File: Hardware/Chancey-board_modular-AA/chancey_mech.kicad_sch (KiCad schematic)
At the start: 81 parts

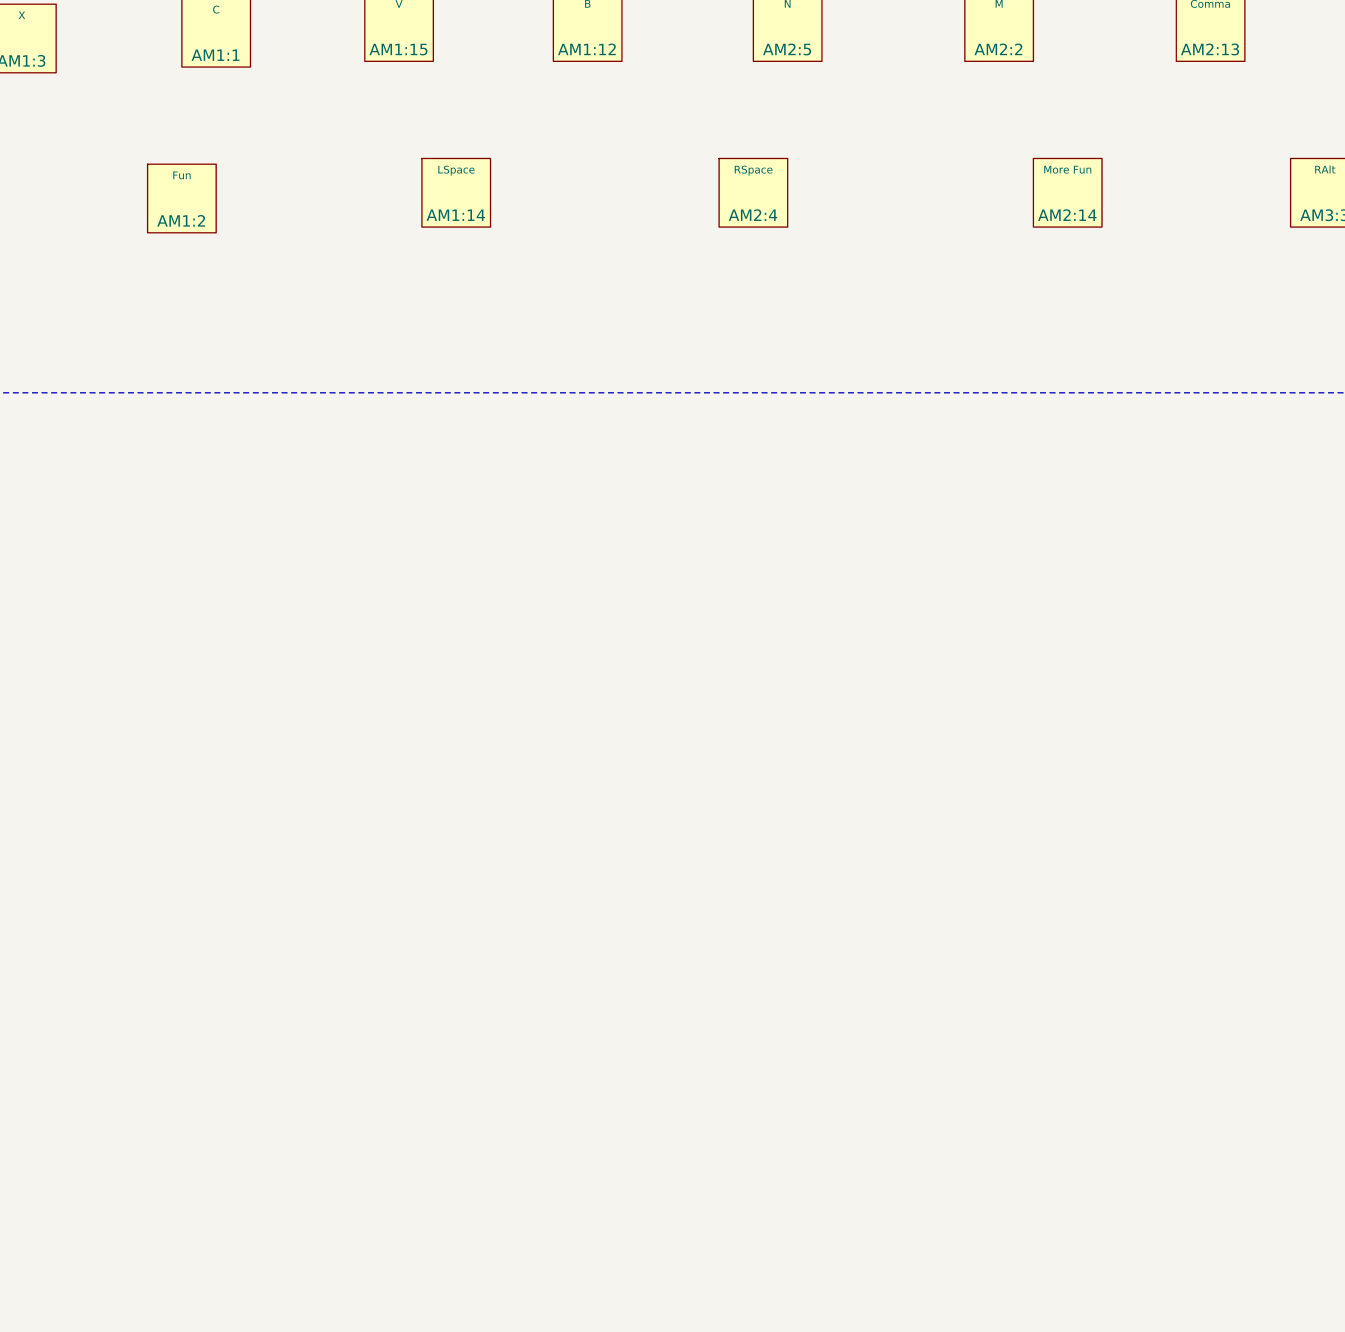
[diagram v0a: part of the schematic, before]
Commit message: Changed many global labels to hierarchical and local labels.
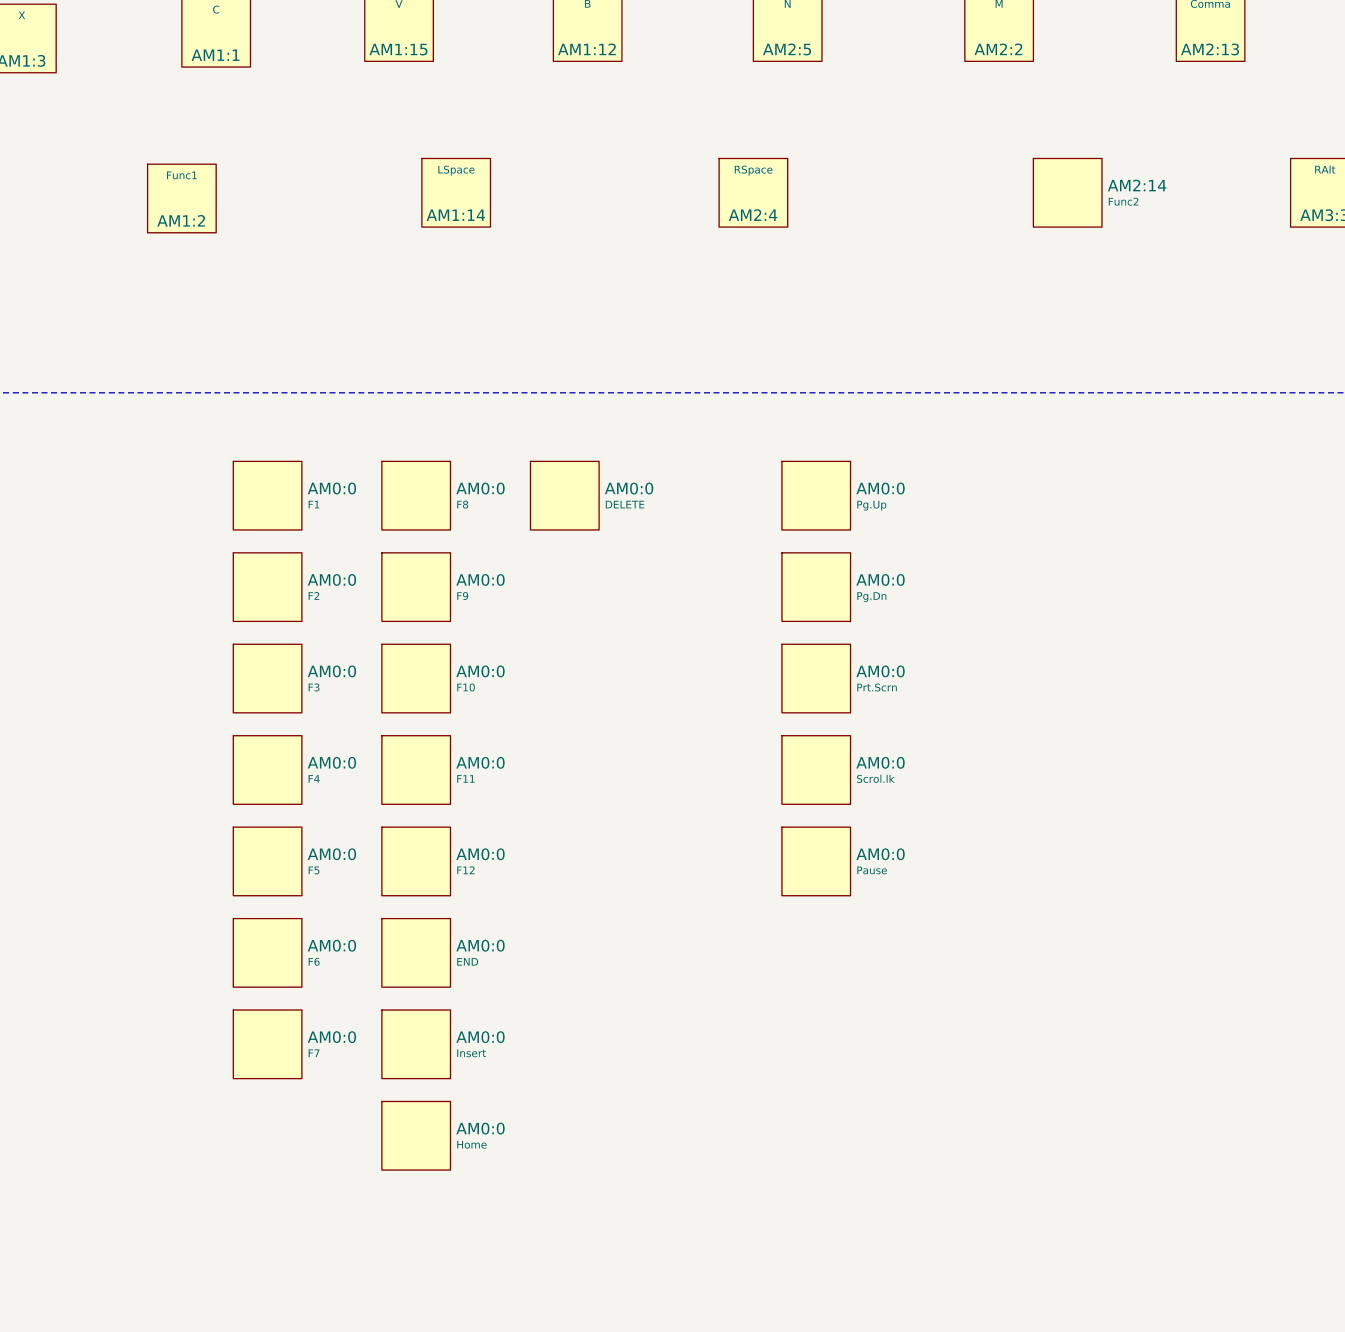
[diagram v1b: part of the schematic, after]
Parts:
- added AM0:0: F3, Chancey_modular:VoidSwitch_1u_SMD, symbol voidswitch:VoidSwitch
- added AM0:0: DELETE, Chancey_modular:VoidSwitch_1u_SMD, symbol voidswitch:VoidSwitch
- added AM0:0: F4, Chancey_modular:VoidSwitch_1u_SMD, symbol voidswitch:VoidSwitch
- added AM0:0: Home, Chancey_modular:VoidSwitch_1u_SMD, symbol voidswitch:VoidSwitch
- added AM0:0: F6, Chancey_modular:VoidSwitch_1u_SMD, symbol voidswitch:VoidSwitch
- added AM0:0: F5, Chancey_modular:VoidSwitch_1u_SMD, symbol voidswitch:VoidSwitch
- added AM0:0: Prt.Scrn, Chancey_modular:VoidSwitch_1u_SMD, symbol voidswitch:VoidSwitch
- added AM0:0: F2, Chancey_modular:VoidSwitch_1u_SMD, symbol voidswitch:VoidSwitch
- added AM0:0: Scrol.lk, Chancey_modular:VoidSwitch_1u_SMD, symbol voidswitch:VoidSwitch
- added AM0:0: Pause, Chancey_modular:VoidSwitch_1u_SMD, symbol voidswitch:VoidSwitch
- added AM0:0: Pg.Dn, Chancey_modular:VoidSwitch_1u_SMD, symbol voidswitch:VoidSwitch
- added AM0:0: F11, Chancey_modular:VoidSwitch_1u_SMD, symbol voidswitch:VoidSwitch
- added AM0:0: F10, Chancey_modular:VoidSwitch_1u_SMD, symbol voidswitch:VoidSwitch
- added AM0:0: END, Chancey_modular:VoidSwitch_1u_SMD, symbol voidswitch:VoidSwitch
- added AM0:0: F9, Chancey_modular:VoidSwitch_1u_SMD, symbol voidswitch:VoidSwitch
- added AM0:0: F8, Chancey_modular:VoidSwitch_1u_SMD, symbol voidswitch:VoidSwitch
- added AM0:0: F7, Chancey_modular:VoidSwitch_1u_SMD, symbol voidswitch:VoidSwitch
- added AM0:0: F12, Chancey_modular:VoidSwitch_1u_SMD, symbol voidswitch:VoidSwitch
- added AM0:0: Pg.Up, Chancey_modular:VoidSwitch_1u_SMD, symbol voidswitch:VoidSwitch
- added AM0:0: F1, Chancey_modular:VoidSwitch_1u_SMD, symbol voidswitch:VoidSwitch
- added AM0:0: Insert, Chancey_modular:VoidSwitch_1u_SMD, symbol voidswitch:VoidSwitch
- AM0:0, AM0:1, AM0:15, AM3:3: footprint void_switch:VoidSwitch_1.25u_SMD -> Chancey_modular:VoidSwitch_1u_SMD
- AM0:10, AM0:11, AM0:12, AM0:13, AM0:14, AM0:2, AM0:3, AM0:4, AM0:5, AM0:6, AM0:7, AM0:8, AM0:9, AM1:0, AM1:1, AM1:10, AM1:11, AM1:12, AM1:13, AM1:14, AM1:15, AM1:3, AM1:4, AM1:5, AM1:6, AM1:7, AM1:8, AM1:9, AM2:10, AM2:11, AM2:12, AM2:13, AM2:2, AM2:3, AM2:4, AM2:5, AM2:6, AM2:7, AM2:8, AM2:9, AM3:1, AM3:10, AM3:11, AM3:12, AM3:13, AM3:14, AM3:2, AM3:4, AM3:5, AM3:6, AM3:7, AM3:8, AM3:9, AM4:0, AM4:1, AM4:12, AM4:13, AM4:14, AM4:15, AM4:3, AM4:4, AM4:5, AM4:6, AM4:7: footprint void_switch:VoidSwitch_1u_SMD -> Chancey_modular:VoidSwitch_1u_SMD
- AM1:2: value Fun -> Func1; footprint void_switch:VoidSwitch_1.25u_SMD -> Chancey_modular:VoidSwitch_1u_SMD
- AM2:14: value More Fun -> Func2; footprint void_switch:VoidSwitch_1.25u_SMD -> Chancey_modular:VoidSwitch_1u_SMD
